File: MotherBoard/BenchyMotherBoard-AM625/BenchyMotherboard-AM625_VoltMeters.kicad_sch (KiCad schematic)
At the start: 110 parts, among them J20 VOLT METER CONN, U39 INA826AIDRGR, U40 INA826AIDRGR, U41 INA826AIDRGR, U57 INA826AIDRGR, U60 INA826AIDRGR, U61 INA826AIDRGR, U62 INA826AIDRGR, U63 INA826AIDRGR, U64 AD7689ACPZ, U73 TPS7A9401DSCR

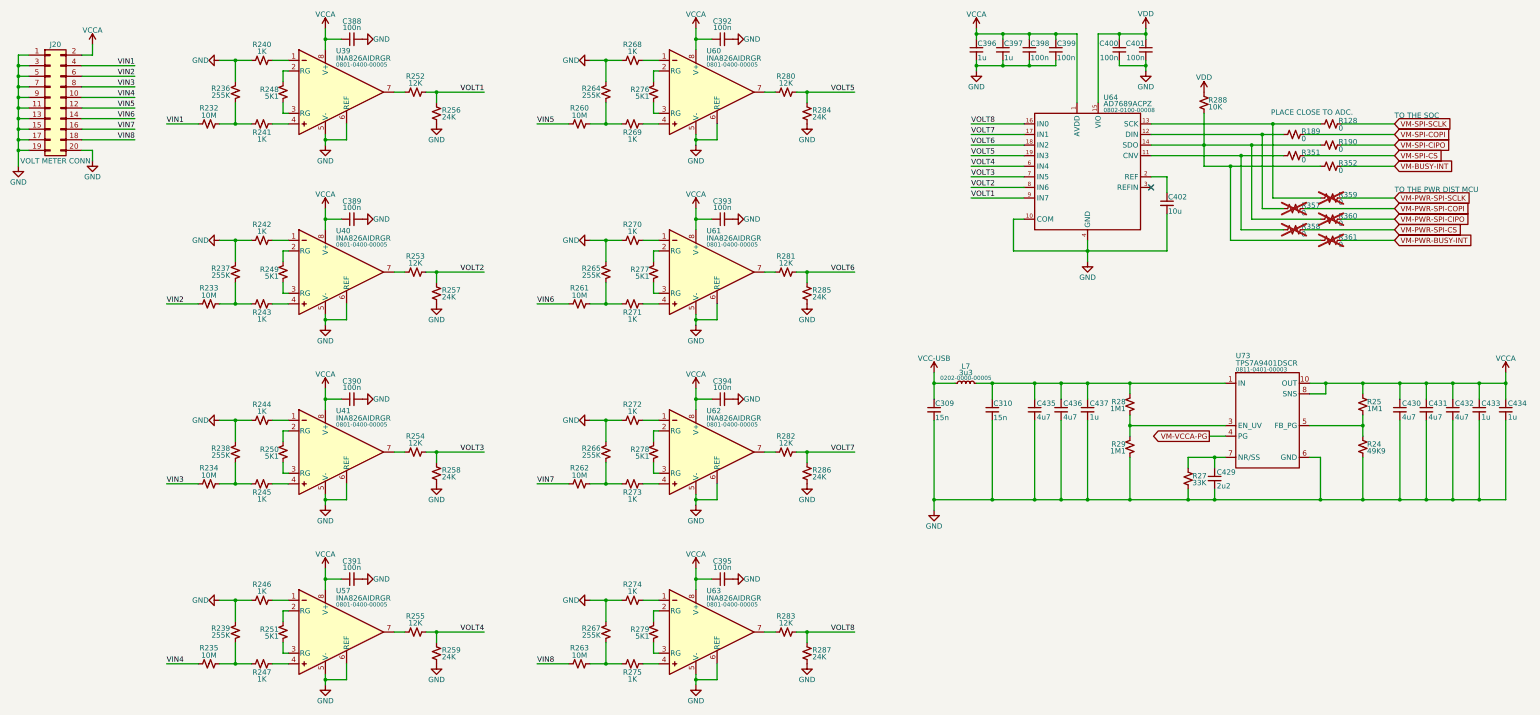
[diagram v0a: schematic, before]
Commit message: Schematic capture mostly complete. Starting PCB layout
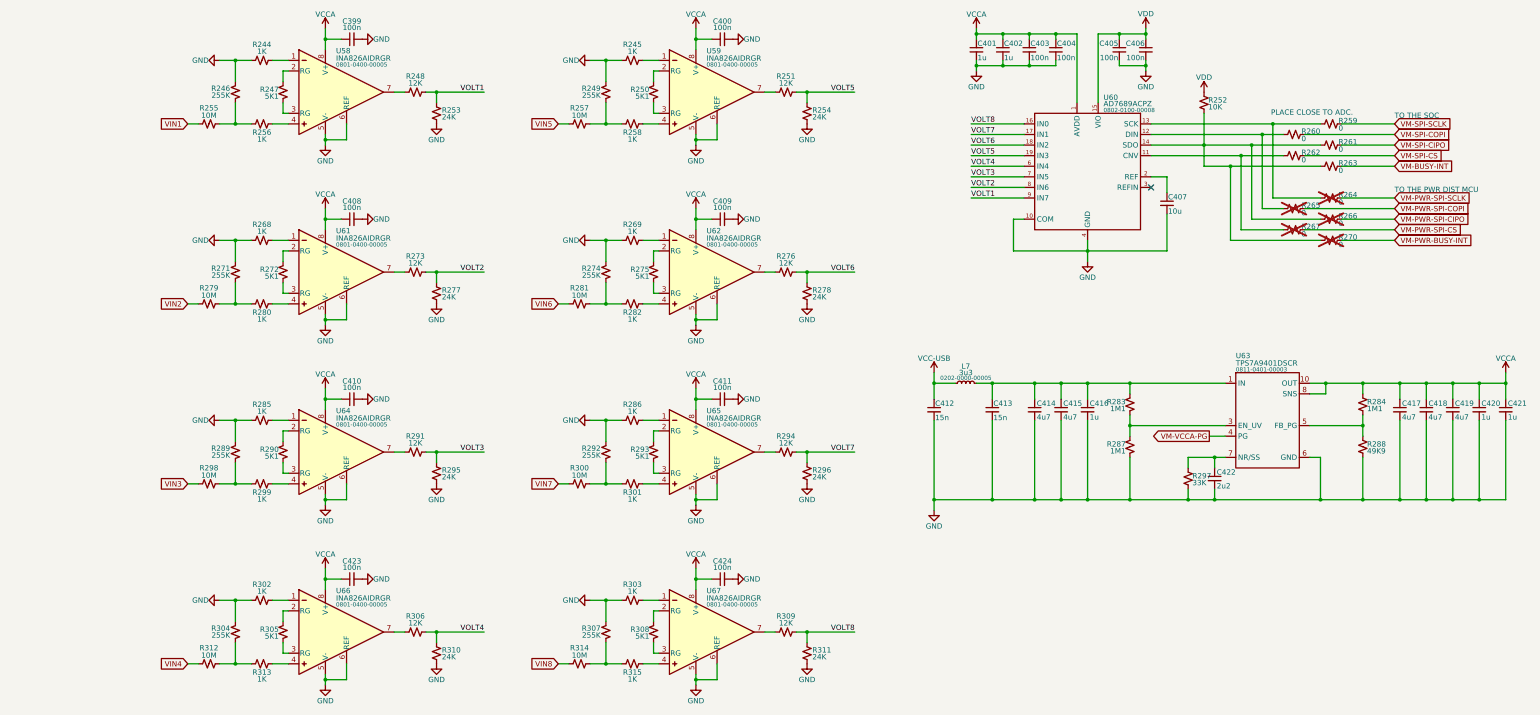
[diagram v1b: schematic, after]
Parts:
- removed J20: VOLT METER CONN, Connector_PinHeader_2.54mm:PinHeader_2x10_P2.54mm_Horizontal, symbol Connector_Generic:Conn_02x10_Odd_Even
- renumbered C388 to C399, C392 to C400, C396 to C401, C397 to C402, C398 to C403, C399 to C404, C400 to C405, C401 to C406, C402 to C407, C389 to C408, C393 to C409, C390 to C410, C394 to C411, C309 to C412, C310 to C413, C435 to C414, C436 to C415, C437 to C416, C430 to C417, C431 to C418, C432 to C419, C433 to C420, C434 to C421, C429 to C422, C391 to C423, C395 to C424, R240 to R244, R268 to R245, R236 to R246, R248 to R247, R252 to R248, R264 to R249, R276 to R250, R280 to R251, R288 to R252, R256 to R253, R284 to R254, R232 to R255, R241 to R256, R260 to R257, R269 to R258, R128 to R259, R189 to R260, R190 to R261, R351 to R262, R352 to R263, R359 to R264, R357 to R265, R360 to R266, R358 to R267, R242 to R268, R270 to R269, R361 to R270, R237 to R271, R249 to R272, R253 to R273, R265 to R274, R277 to R275, R281 to R276, R257 to R277, R285 to R278, R233 to R279, R243 to R280, R261 to R281, R271 to R282, R28 to R283, R25 to R284, R244 to R285, R272 to R286, R29 to R287, R24 to R288, R238 to R289, R250 to R290, R254 to R291, R266 to R292, R278 to R293, R282 to R294, R258 to R295, R286 to R296, R27 to R297, R234 to R298, R245 to R299, R262 to R300, R273 to R301, R246 to R302, R274 to R303, R239 to R304, R251 to R305, R255 to R306, R267 to R307, R279 to R308, R283 to R309, R259 to R310, R287 to R311, R235 to R312, R247 to R313, R263 to R314, R275 to R315, U39 to U58, U60 to U59, U64 to U60, U40 to U61, U61 to U62, U73 to U63, U41 to U64, U62 to U65, U57 to U66, U63 to U67
